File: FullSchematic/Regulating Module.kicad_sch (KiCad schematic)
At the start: 9 parts, among them U2 LM1117-3.3

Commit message: generated files
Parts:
- TP15: JLCPCB Part # N/A -> (none)
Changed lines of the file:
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@@
       (effects (font (size 1.27 1.27)) hide)
     )
-    (property "JLCPCB Part #" "N/A" (at 113.03 92.71 0)
+    (property "JLCPCB Part #" "" (at 113.03 92.71 0)
       (effects (font (size 1.27 1.27)) hide)
     )
@@
       (effects (font (size 1.27 1.27)) hide)
     )
-    (property "JLCPCB Part #" "N/A" (at 173.99 92.71 0)
-      (effects (font (size 1.27 1.27)) hide)
-    )
+    (property "JLCPCB Part #" "" (at 173.99 92.71 0)
+      (effects (font (size 1.27 1.27)) hide)
+    )

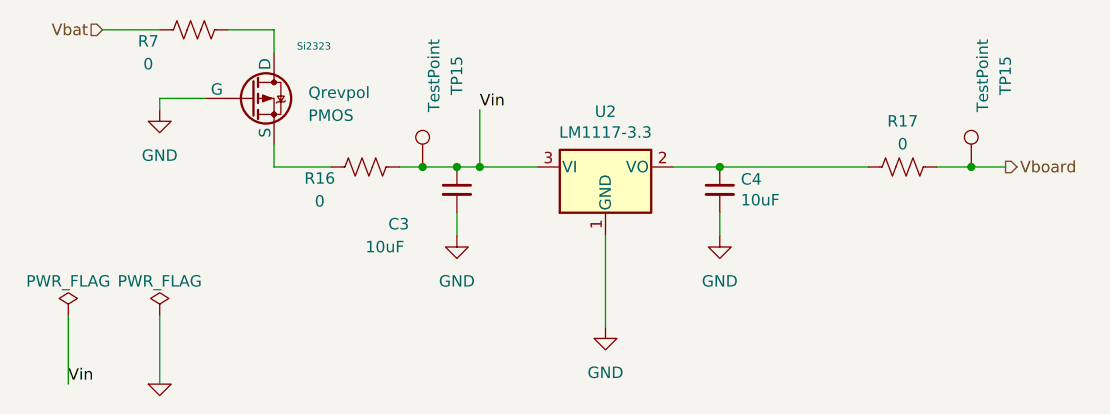
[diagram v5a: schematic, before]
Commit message: Decreased Price
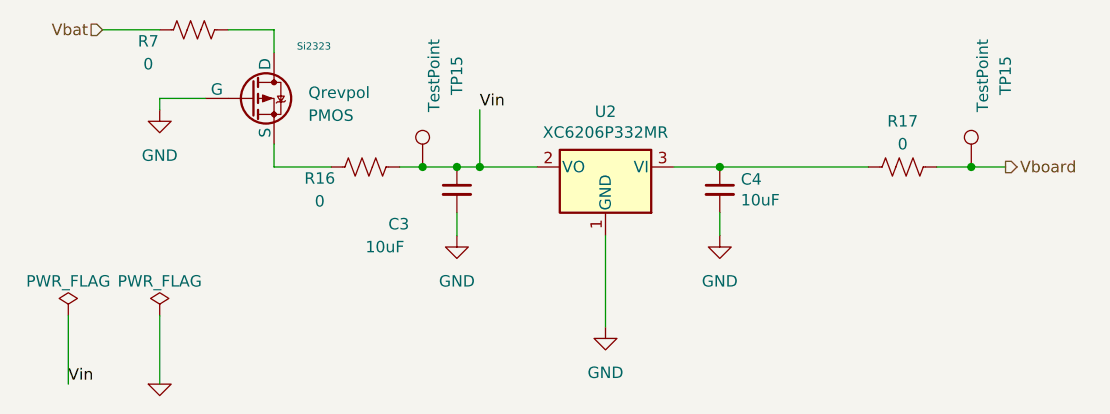
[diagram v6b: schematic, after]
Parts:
- C3, C4: footprint Capacitor_SMD:C_0603_1608Metric -> Capacitor_SMD:C_1206_3216Metric; JLCPCB Part # C1691 -> C13585
- Qrevpol: JLCPCB Part # C5337196 -> C10487
- U2: value LM1117-3.3 -> XC6206P332MR; footprint Package_TO_SOT_SMD:SOT-223 -> Package_TO_SOT_SMD:SOT-23-3; JLCPCB Part # C126027 -> C5446
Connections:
- net Vin: now also U2.2 (VO); no longer U2.3 (VI)
- net at C4.1, R17.1: now also U2.3 (VI); no longer U2.2 (VO)
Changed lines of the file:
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@@
     (effects (font (size 1.27 1.27)) (justify right))
   )
-  (symbol (lib_id "Power module-rescue:LM1117-3.3-Regulator_Linear") (at 133.35 92.71 0) (unit 1)
+  (symbol (lib_id "Power module-rescue:LM1117-3.3-Regulator_Linear") (at 133.35 92.71 0) (mirror y) (unit 1)
     (in_bom yes) (on_board yes) (dnp no)
     (property "Reference" "U2" (at 133.35 86.5632 0)
       (effects (font (size 1.27 1.27)))
     )
-    (property "Value" "LM1117-3.3" (at 133.35 88.8746 0)
-      (effects (font (size 1.27 1.27)))
-    )
-    (property "Footprint" "Package_TO_SOT_SMD:SOT-223" (at 133.35 92.71 0)
+    (property "Value" "XC6206P332MR" (at 133.35 88.8746 0)
+      (effects (font (size 1.27 1.27)))
+    )
+    (property "Footprint" "Package_TO_SOT_SMD:SOT-23-3" (at 133.35 92.71 0)
       (effects (font (size 1.27 1.27)) hide)
     )
@@
       (effects (font (size 1.27 1.27)) hide)
     )
-    (property "JLCPCB Part #" "C126027" (at 133.35 92.71 0)
+    (property "JLCPCB Part #" "C5446" (at 133.35 92.71 0)
       (effects (font (size 1.27 1.27)) hide)
     )
@@
       (effects (font (size 1.27 1.27)) (justify left))
     )
-    (property "Footprint" "Capacitor_SMD:C_0603_1608Metric" (at 116.84 95.25 0)
+    (property "Footprint" "Capacitor_SMD:C_1206_3216Metric" (at 116.84 95.25 0)
       (effects (font (size 1.27 1.27)) hide)
     )
@@
       (effects (font (size 1.27 1.27)) hide)
     )
-    (property "JLCPCB Part #" "C1691" (at 116.84 95.25 0)
+    (property "JLCPCB Part #" "C13585" (at 116.84 95.25 0)
       (effects (font (size 1.27 1.27)) hide)
     )
@@
       (effects (font (size 1.27 1.27)) (justify left))
     )
-    (property "Footprint" "Capacitor_SMD:C_0603_1608Metric" (at 146.05 95.25 0)
+    (property "Footprint" "Capacitor_SMD:C_1206_3216Metric" (at 146.05 95.25 0)
       (effects (font (size 1.27 1.27)) hide)
     )
@@
       (effects (font (size 1.27 1.27)) hide)
     )
-    (property "JLCPCB Part #" "C1691" (at 146.05 95.25 0)
+    (property "JLCPCB Part #" "C13585" (at 146.05 95.25 0)
       (effects (font (size 1.27 1.27)) hide)
     )
@@
       (effects (font (size 1.27 1.27)) hide)
     )
-    (property "JLCPCB Part #" "C5337196" (at 93.98 85.09 0)
-      (effects (font (size 1.27 1.27)) hide)
-    )
+    (property "JLCPCB Part #" "C10487" (at 93.98 85.09 0)
+      (effects (font (size 1.27 1.27)) hide)
+    )

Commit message: Uploaded final board design
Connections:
- net Vin: now also U2.3 (VI); no longer U2.2 (VO)
- net at C4.1, R17.1: now also U2.2 (VO); no longer U2.3 (VI)
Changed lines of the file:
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@@
     (effects (font (size 1.27 1.27)) (justify right))
   )
-  (symbol (lib_id "Power module-rescue:LM1117-3.3-Regulator_Linear") (at 133.35 92.71 0) (mirror y) (unit 1)
+  (symbol (lib_id "Power module-rescue:LM1117-3.3-Regulator_Linear") (at 133.35 92.71 0) (unit 1)
     (in_bom yes) (on_board yes) (dnp no)
     (property "Reference" "U2" (at 133.35 86.5632 0)
